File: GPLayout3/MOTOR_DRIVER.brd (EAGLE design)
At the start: 162.2 x 45.4 mm, 95 parts, among them T1 2N2222, T2 2N2222, U7 ATMEGA328P_TQFP, Y1 16MHz

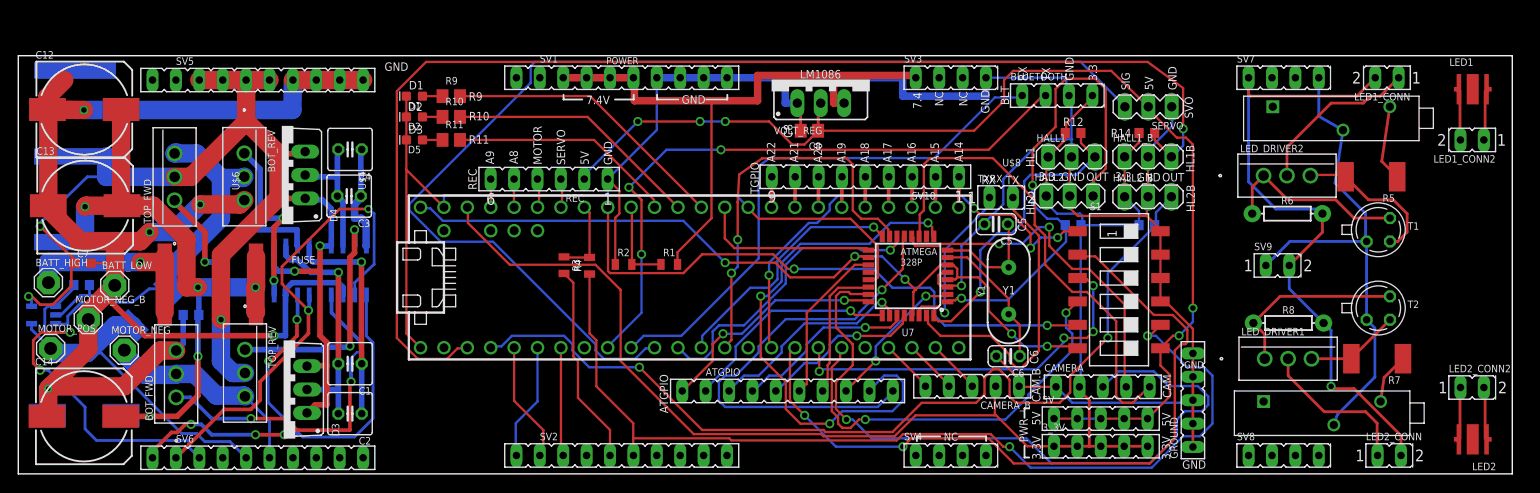
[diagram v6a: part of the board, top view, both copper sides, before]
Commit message: Added more silkscreen
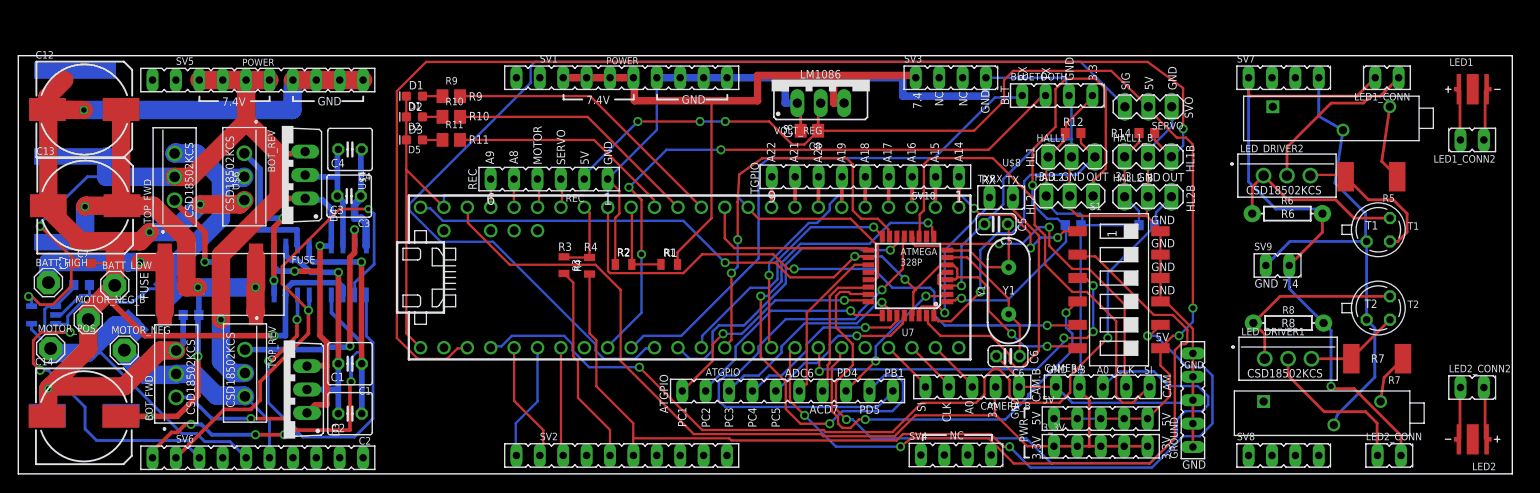
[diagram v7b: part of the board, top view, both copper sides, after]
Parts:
- moved SV4 0.56 mm to (103.1, 2.05)
- moved CAMERA_B 0.08 mm to (103.5, 9.44)
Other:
- board text added: "A0"
- board text added: "ACD7"
- board text added: "ADC6"
- board text added: "C1"
- board text added: "C2"
- board text added: "C3"
- board text added: "C4"
- board text added: "C7"
- board text added: "CLK"
- board text added: "FUSE"
- board text added: "PB1"
- board text added: "PC1"
- board text added: "PC2"
- board text added: "PC3"
- board text added: "PC4"
- board text added: "PC5"
- board text added: "PD4"
- board text added: "PD5"
- board text added: "R1"
- board text added: "R2"
- board text added: "R3"
- board text added: "R4"
- board text added: "R6"
- board text added: "R7"
- board text added: "R8"
- board text added: "SI"
- board text added: "T1"
- board text added: "T2"

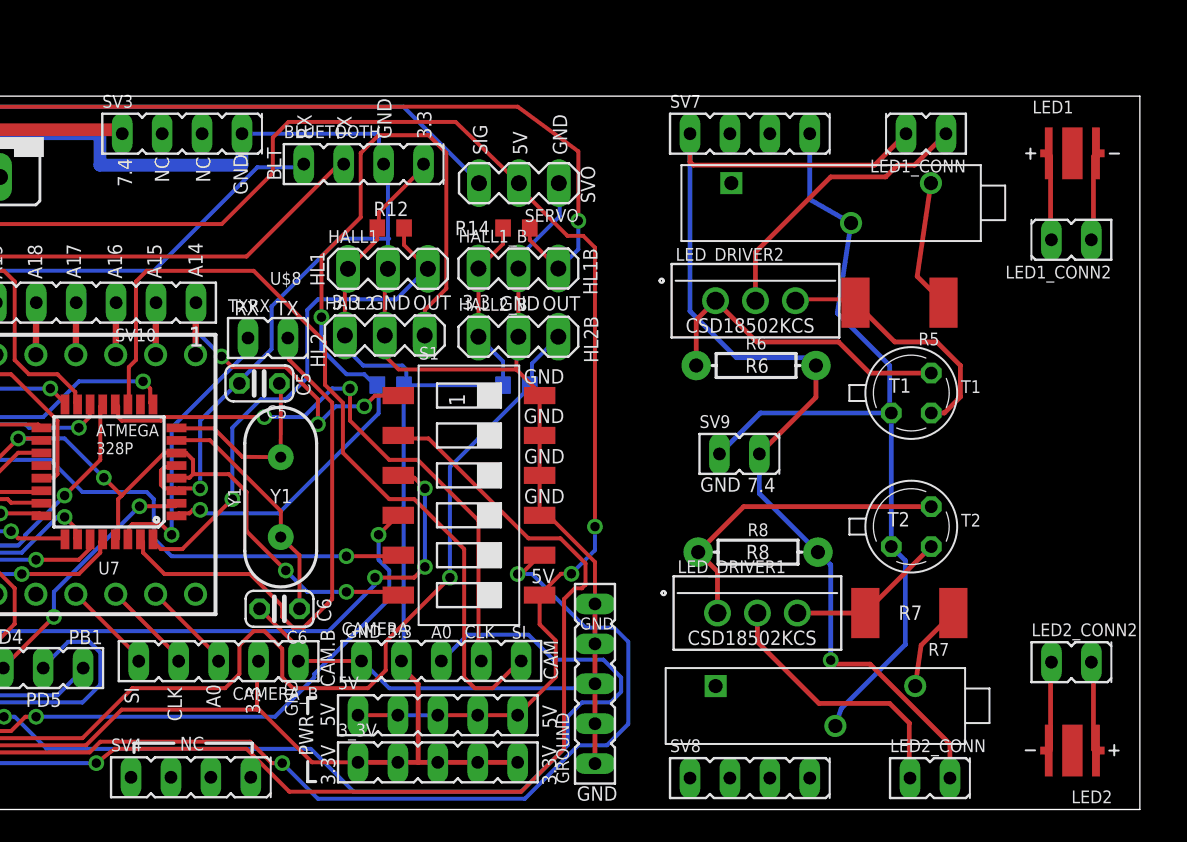
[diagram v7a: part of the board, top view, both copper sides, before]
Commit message: added thermal things for LEDs
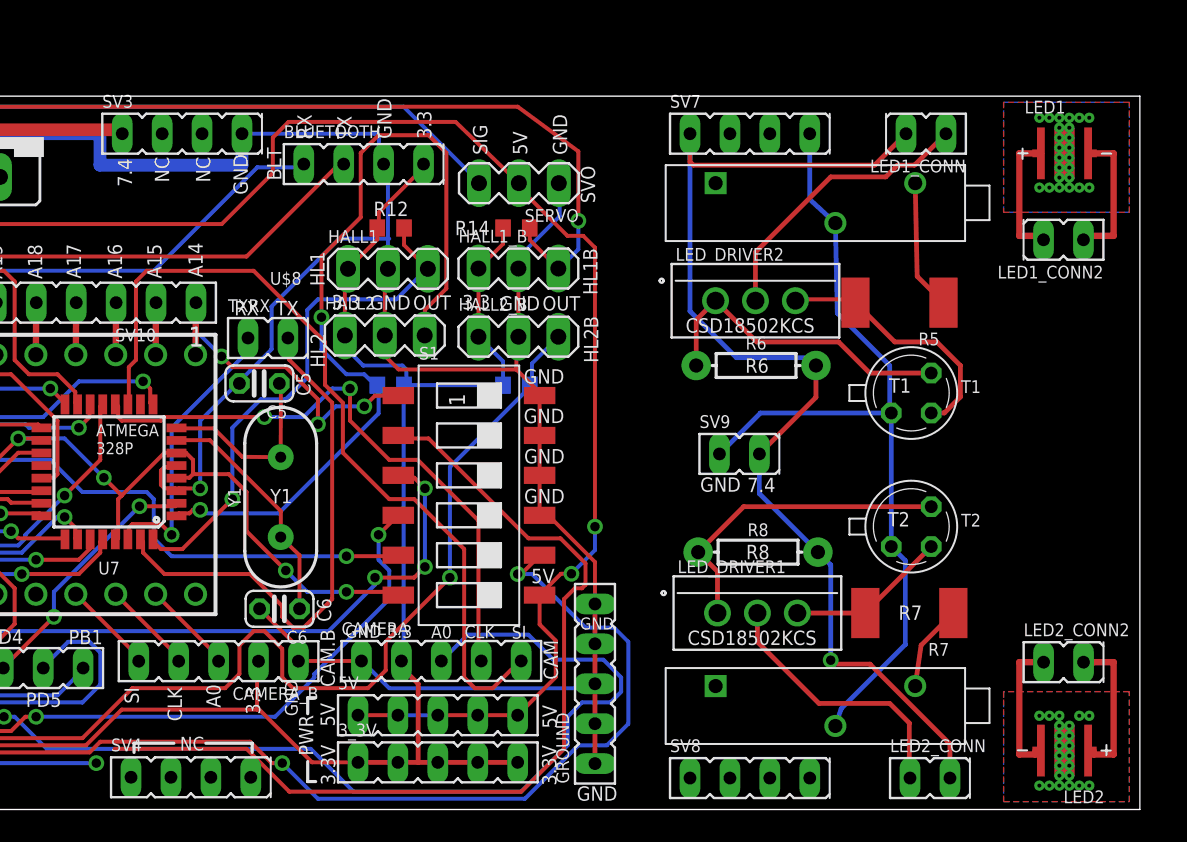
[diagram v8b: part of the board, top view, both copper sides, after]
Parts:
- moved U$7 1.00 mm to (132.0, 41.0)
- moved LED1 0.50 mm to (157.4, 41.8)
- moved LED1_CONN2 0.50 mm to (153.5, 36.2)
- moved LED2 0.50 mm to (157.4, 3.75)
- moved LED2_CONN2 0.50 mm to (161.1, 9.38)
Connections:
- new net THERM2: LED2.THERMAL
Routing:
- net LED2HI: track 6.19 -> 9.96 mm
- net LED1LO: track 6.01 -> 9.04 mm
- net LED1HI: track 5.94 -> 8.66 mm
- net LED2LO: track 6.12 -> 8.69 mm
- net SW2: track 80.3 -> 78.9 mm
- net GND_TOP2: track 54.8 -> 54.0 mm
- added copper zone on layer 1, net THERM1
- added copper zone on layer 16, net THERM1
- added copper zone on layer 1, net THERM2
- added copper zone on layer 16, net THERM2
